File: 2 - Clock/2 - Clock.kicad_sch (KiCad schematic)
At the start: 11 parts, among them J1 BUS 1, J2 RST/CLK TP, SW1 RESET, U1 74AC14, U2 74AC174

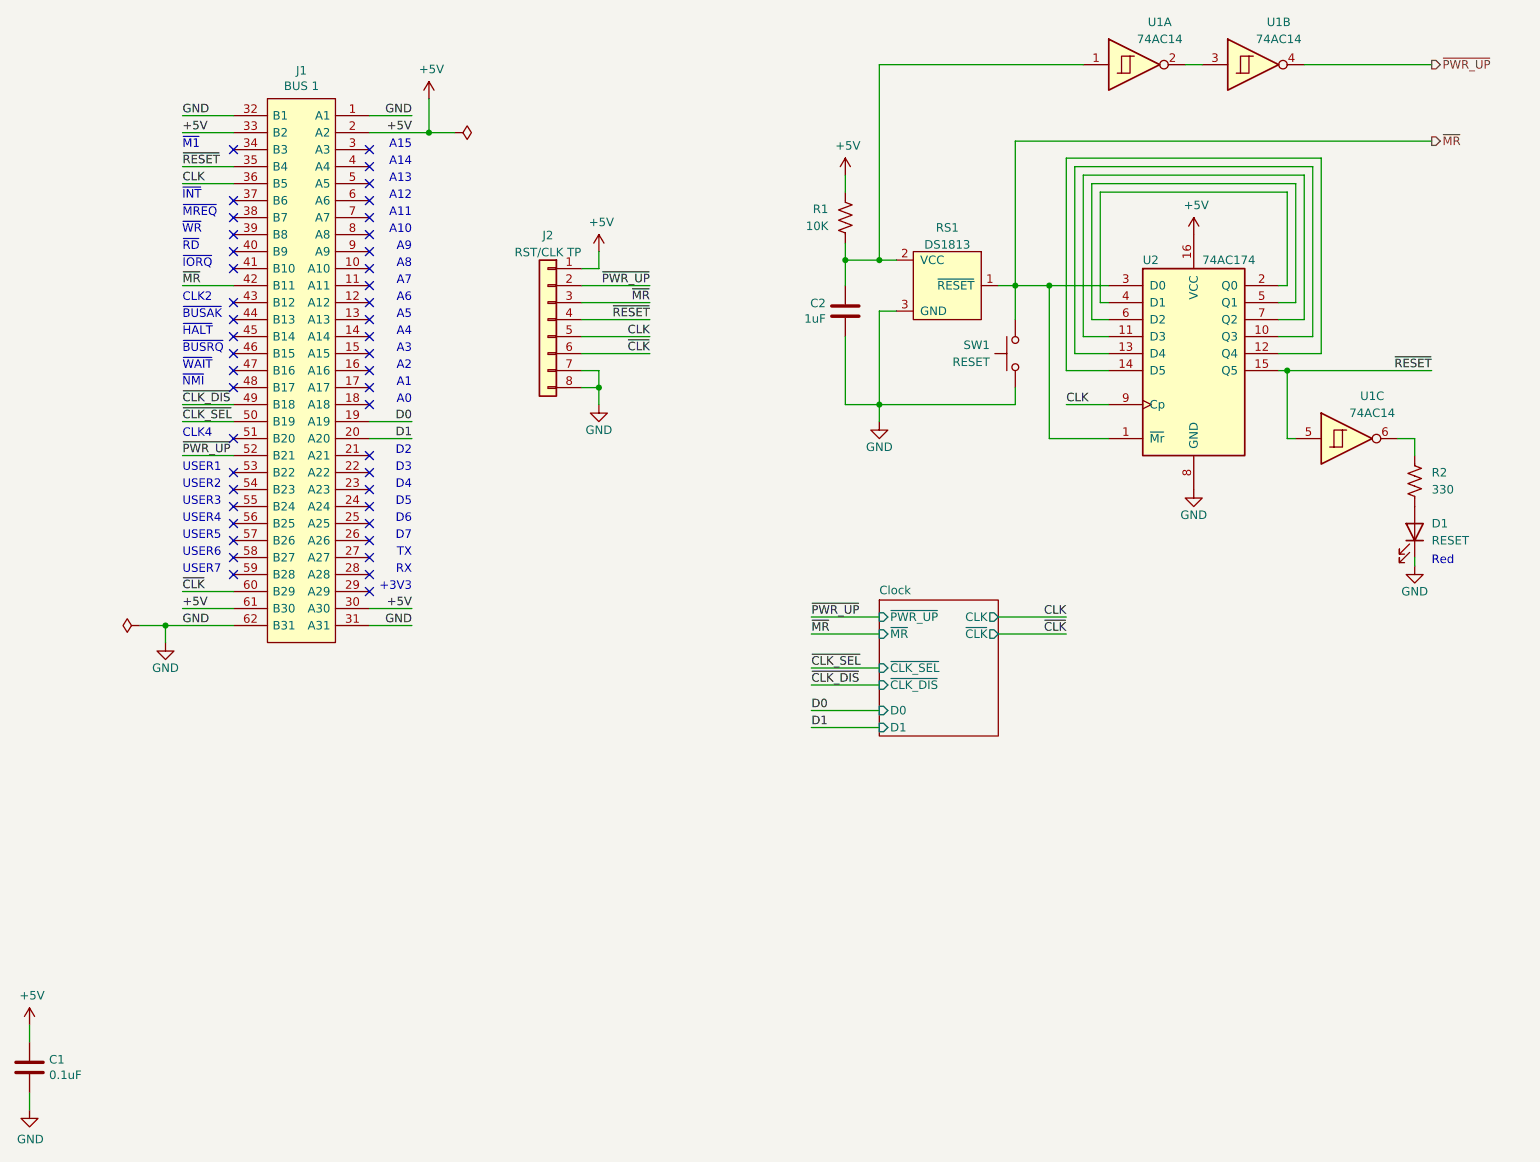
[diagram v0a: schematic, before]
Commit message: Clock card updated
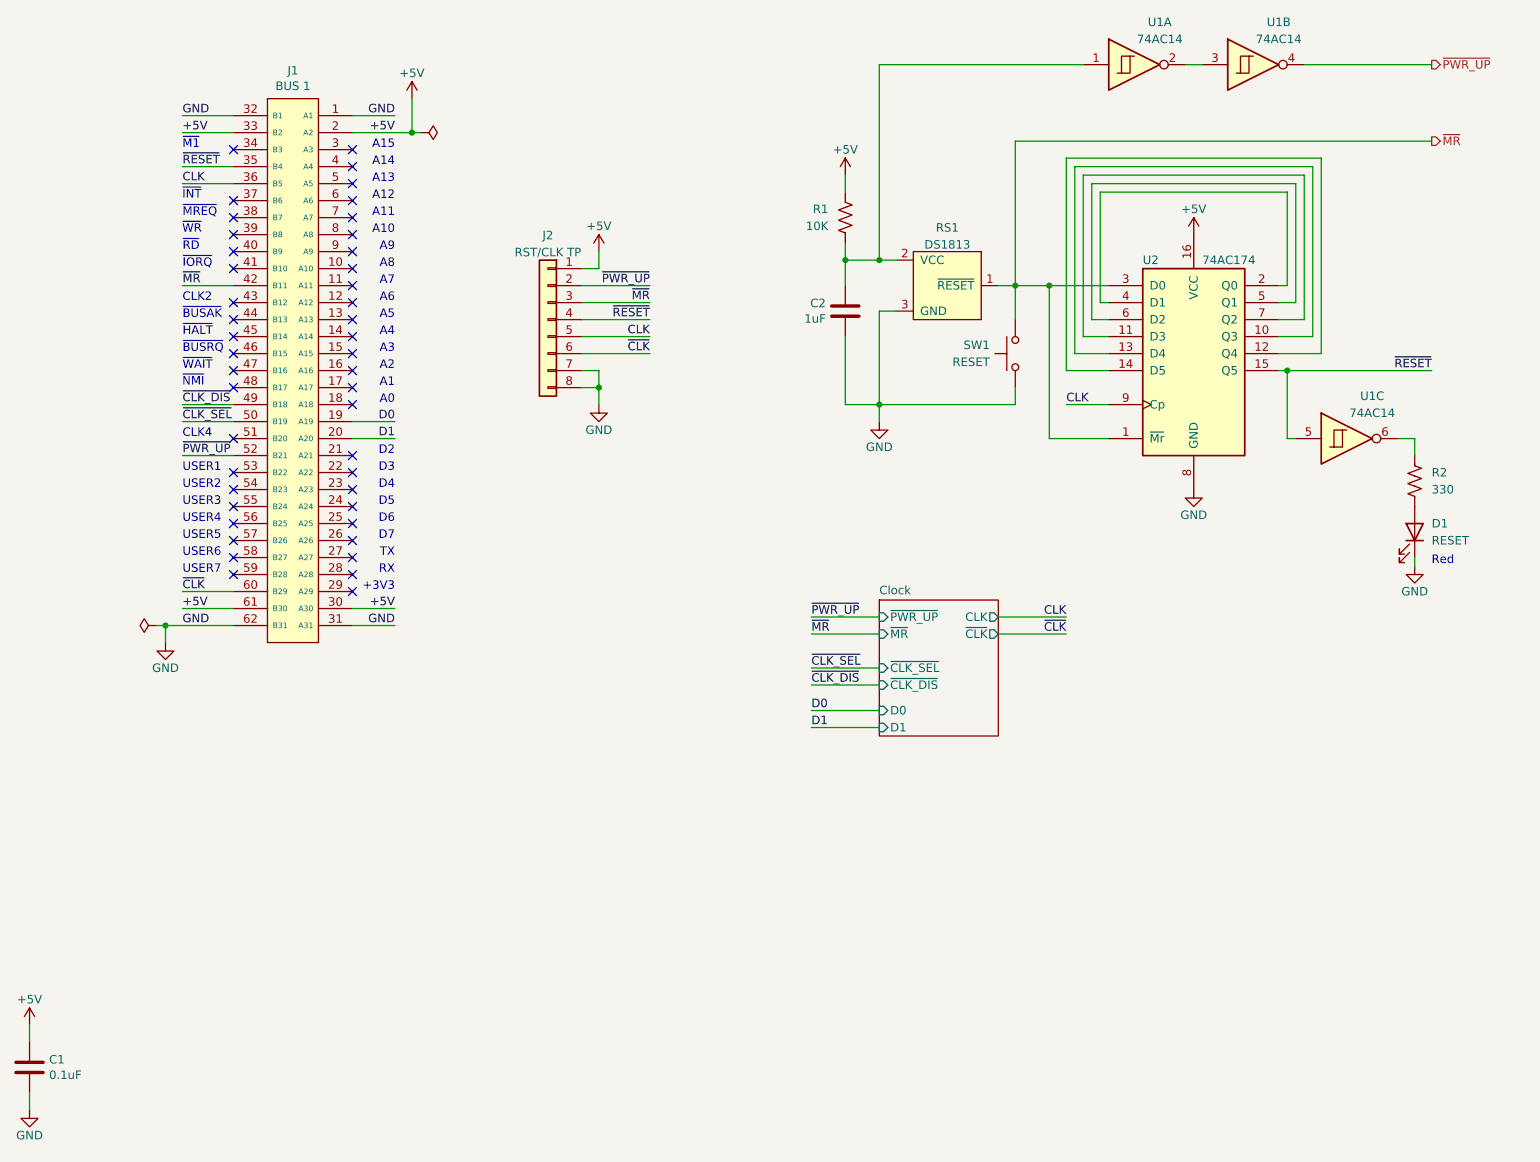
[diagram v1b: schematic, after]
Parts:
- J1: footprint 0 - Library:BUS_XT -> 0_Library:BUS_XT_Proto; symbol 0 - Library:ISA_CARD_CONNECTOR -> 0_Library:ISA_CARD_CONNECTOR_8BIT
- RS1: symbol 0 - Library:DS1813 -> 0_Library:DS1813
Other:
- moved on the sheet: J1

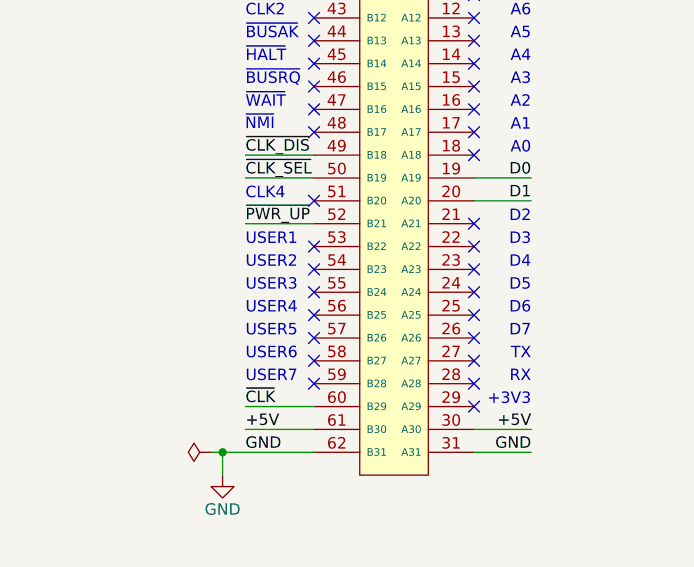
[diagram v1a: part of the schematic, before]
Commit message: Added serial card, still needs work
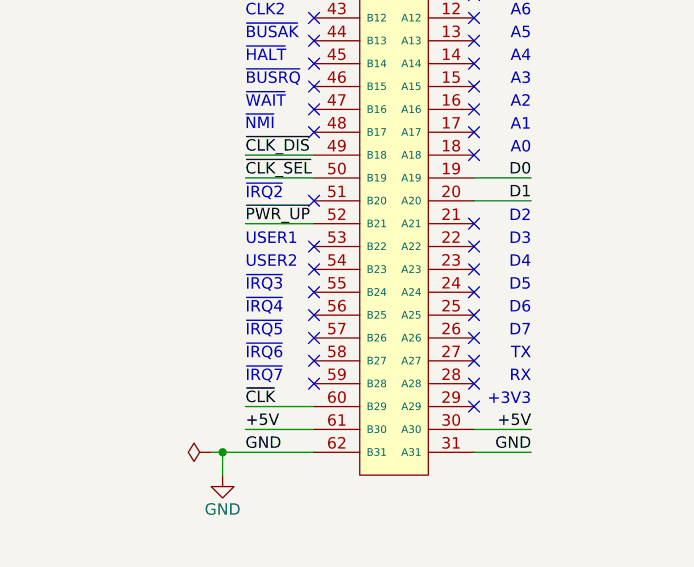
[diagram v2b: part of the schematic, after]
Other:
- note added: "~{IRQ2}"
- note added: "~{IRQ3}"
- note added: "~{IRQ4}"
- note added: "~{IRQ5}"
- note added: "~{IRQ6}"
- note added: "~{IRQ7}"
- note removed: "CLK4"
- note removed: "USER3"
- note removed: "USER4"
- note removed: "USER5"
- note removed: "USER6"
- note removed: "USER7"
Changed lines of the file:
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@@
     (effects (font (size 1.27 1.27)) (justify right bottom))
   )
-  (text "USER6" (at 40.64 113.03 0)
+  (text "~{IRQ4}" (at 40.64 107.95 0)
     (effects (font (size 1.27 1.27)) (justify left bottom))
   )
@@
     (effects (font (size 1.27 1.27)) (justify left bottom))
   )
-  (text "USER5" (at 40.64 110.49 0)
-    (effects (font (size 1.27 1.27)) (justify left bottom))
-  )
   (text "A9" (at 72.39 67.31 0)
     (effects (font (size 1.27 1.27)) (justify right bottom))
@@
   (text "A4" (at 72.39 80.01 0)
     (effects (font (size 1.27 1.27)) (justify right bottom))
+  )
+  (text "~{IRQ7}" (at 40.64 115.57 0)
+    (effects (font (size 1.27 1.27)) (justify left bottom))
   )
   (text "D2" (at 72.39 97.79 0)
@@
     (effects (font (size 1.27 1.27)) (justify left bottom))
   )
-  (text "USER3" (at 40.64 105.41 0)
+  (text "~{IRQ3}" (at 40.64 105.41 0)
     (effects (font (size 1.27 1.27)) (justify left bottom))
   )
-  (text "CLK4" (at 40.64 95.25 0)
-    (effects (font (size 1.27 1.27)) (justify left bottom))
-  )
-  (text "USER4" (at 40.64 107.95 0)
+  (text "~{IRQ2}" (at 40.64 95.25 0)
     (effects (font (size 1.27 1.27)) (justify left bottom))
   )
@@
     (effects (font (size 1.27 1.27)) (justify left bottom))
   )
+  (text "~{IRQ5}" (at 40.64 110.49 0)
+    (effects (font (size 1.27 1.27)) (justify left bottom))
+  )
   (text "D6" (at 72.39 107.95 0)
     (effects (font (size 1.27 1.27)) (justify right bottom))
+  )
+  (text "~{IRQ6}" (at 40.64 113.03 0)
+    (effects (font (size 1.27 1.27)) (justify left bottom))
   )
   (text "~{INT}" (at 40.5902 59.6337 0)
@@
     (effects (font (size 1.27 1.27)) (justify left bottom))
   )
-  (text "USER7" (at 40.64 115.57 0)
-    (effects (font (size 1.27 1.27)) (justify left bottom))
-  )
